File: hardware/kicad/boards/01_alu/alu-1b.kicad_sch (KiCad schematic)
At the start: 2 parts, among them U21 74AC251

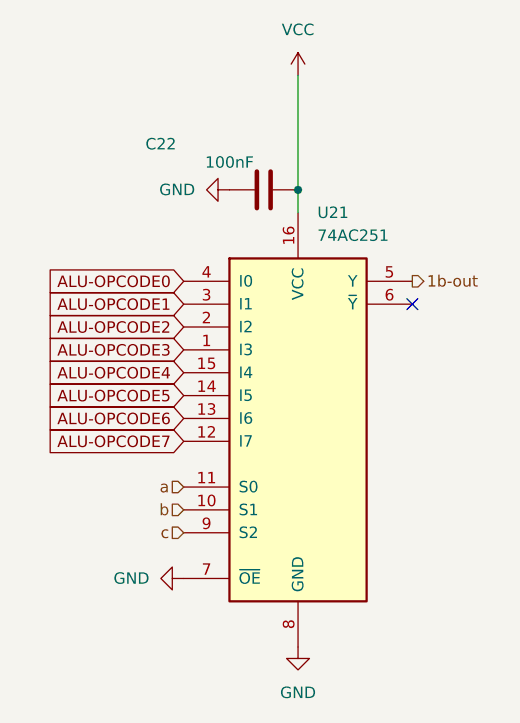
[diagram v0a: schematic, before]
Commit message: arch(alu): replace 251 tri-state MUX with 151 to prevent High-Z faults
Eliminates dead Tri-State functionality on point-to-point traces, preventing potential logic oscillation and chip damage from floating pins. Drive strength and speed are unaffected.

Closes #4
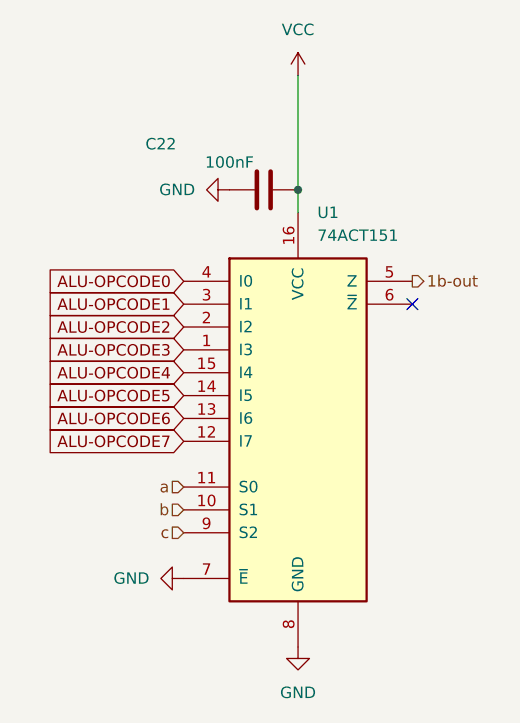
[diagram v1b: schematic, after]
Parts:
- removed U21: 74AC251, Package_SO:SOIC-16_3.9x9.9mm_P1.27mm, symbol 74xx:74LS251
- added U1: 74ACT151, Package_SO:SOIC-16_3.9x9.9mm_P1.27mm, symbol 74xx:74LS151
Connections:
- net 1b-out: now also U1.5 (Z)
- net ALU-OPCODE0: now also U1.4 (I0)
- net ALU-OPCODE1: now also U1.3 (I1)
- net ALU-OPCODE2: now also U1.2 (I2)
- net ALU-OPCODE3: now also U1.1 (I3)
- net ALU-OPCODE4: now also U1.15 (I4)
- net ALU-OPCODE5: now also U1.14 (I5)
- net ALU-OPCODE6: now also U1.13 (I6)
- net ALU-OPCODE7: now also U1.12 (I7)
- net GND: now also U1.7 (~{E}), U1.8 (GND)
- net VCC: now also U1.16 (VCC)
- net a: now also U1.11 (S0)
- net b: now also U1.10 (S1)
- net c: now also U1.9 (S2)
